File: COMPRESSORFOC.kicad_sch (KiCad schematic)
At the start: 85 parts, among them J1 ESP32-PICO-KIT_ESP32-PICO-KIT, J10 3.3V, J11 Pin 1, J12 Pin 2, J13 GND, J2 Fan 1+, J3 Fan 1-, J4 15V+, J5 15VGND, J6 Conn_01x03_Socket, J7 Conn_01x03_Socket, J8 Fan 2+, J9 Fan 2-, Q1 NMOSIPD50R280CEAUMA1, U2 INA240A2DR, U3 INA240A2DR, U5 INA240A2DR

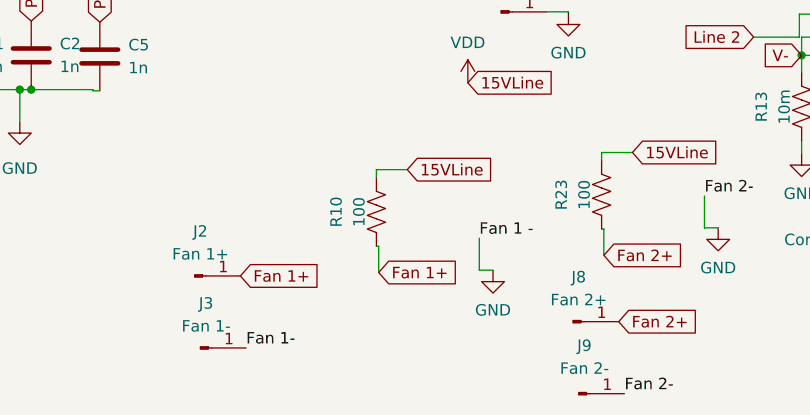
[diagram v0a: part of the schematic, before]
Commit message: workflow typo fix and some erc fixes
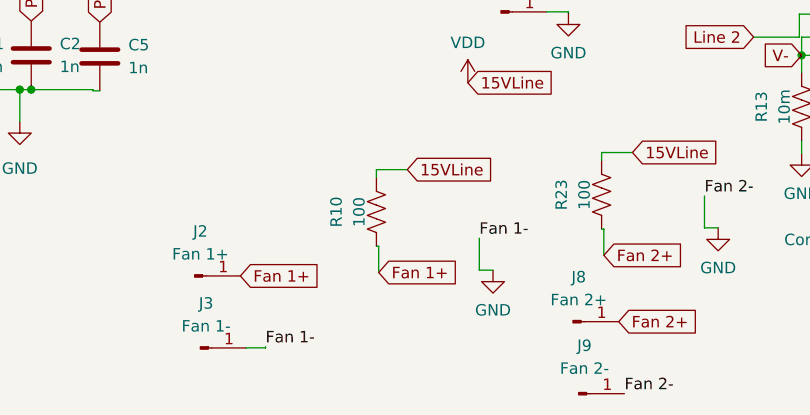
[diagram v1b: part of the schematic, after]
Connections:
- net Fan 1- is gone; now on net GND: J3.1 (Pin_1)
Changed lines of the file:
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@@
+    (stroke (width 0) (type default))
+  )
+  (wire (pts (xy 90.551 188.214) (xy 90.551 188.087))
     (stroke (width 0) (type default))
   )
@@
     (stroke (width 0) (type default))
   )
+  (wire (pts (xy 88.392 188.214) (xy 90.551 188.214))
+    (stroke (width 0) (type default))
+  )
   (wire (pts (xy 128.27 78.74) (xy 132.715 78.74))
     (stroke (width 0) (type default))
@@
     (stroke (width 0) (type default))
   )
-  (label "Fan 1 -" (at 114.3 176.022 0) (fields_autoplaced)
+  (label "Fan 1-" (at 114.3 176.022 0) (fields_autoplaced)
     (effects (font (size 1.27 1.27)) (justify left bottom))
   )
@@
     (effects (font (size 1.27 1.27)) (justify left bottom))
   )
-  (label "Fan 1-" (at 88.392 188.214 0) (fields_autoplaced)
+  (label "Fan 1-" (at 90.551 188.087 0) (fields_autoplaced)
     (effects (font (size 1.27 1.27)) (justify left bottom))
   )

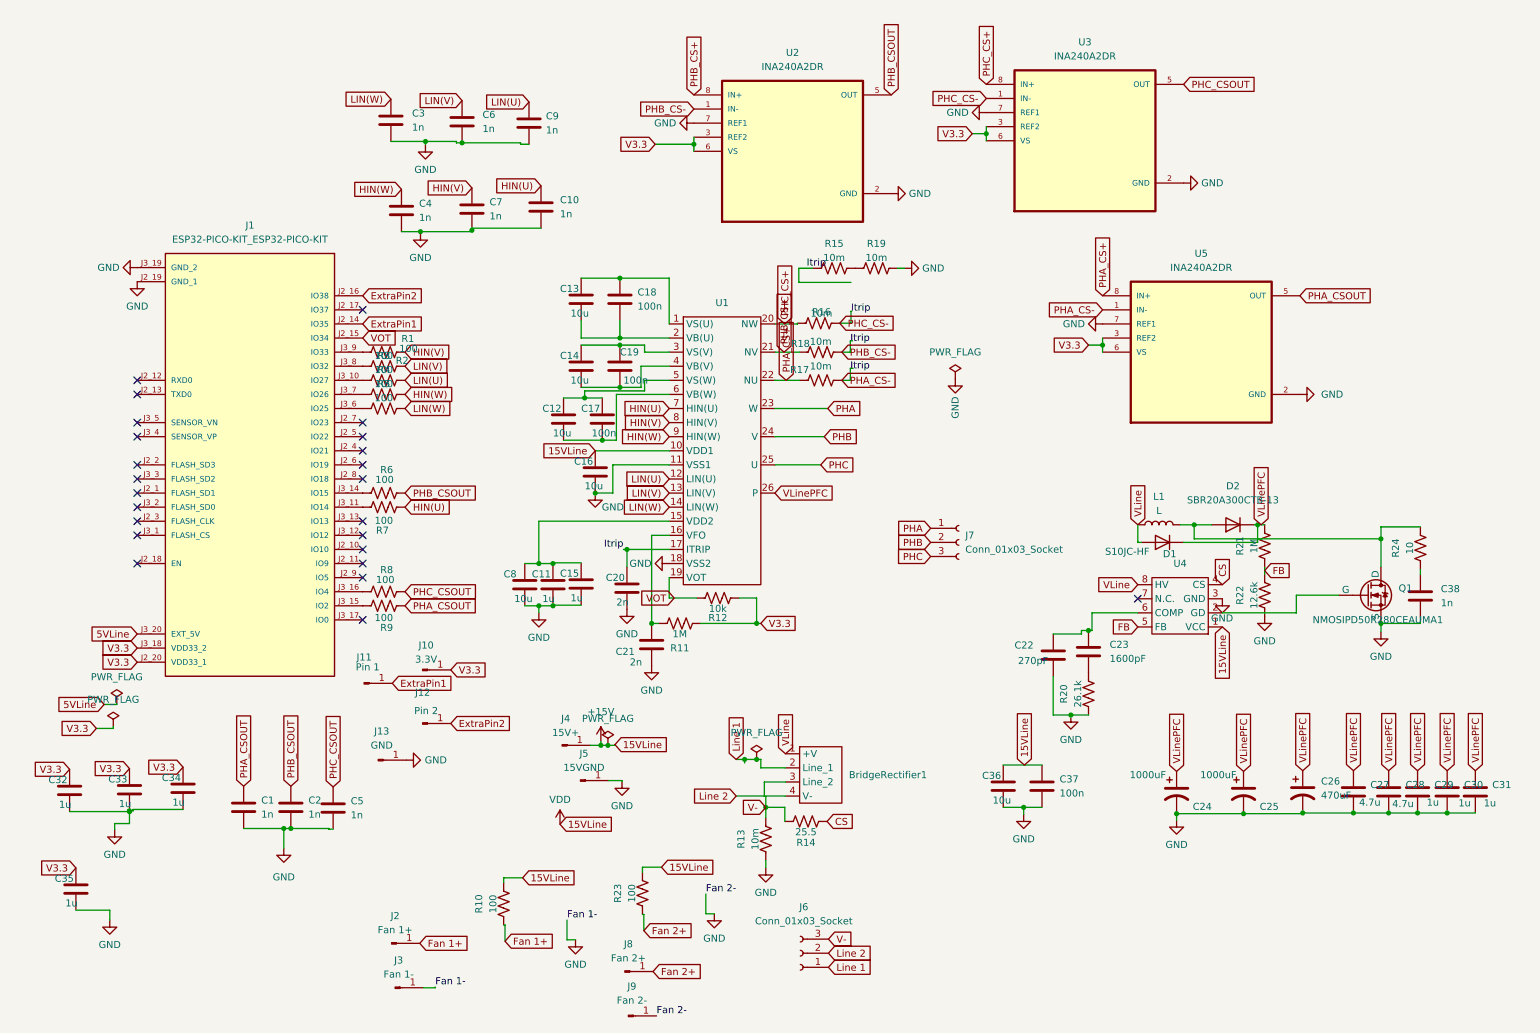
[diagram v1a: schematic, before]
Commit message: revised driver
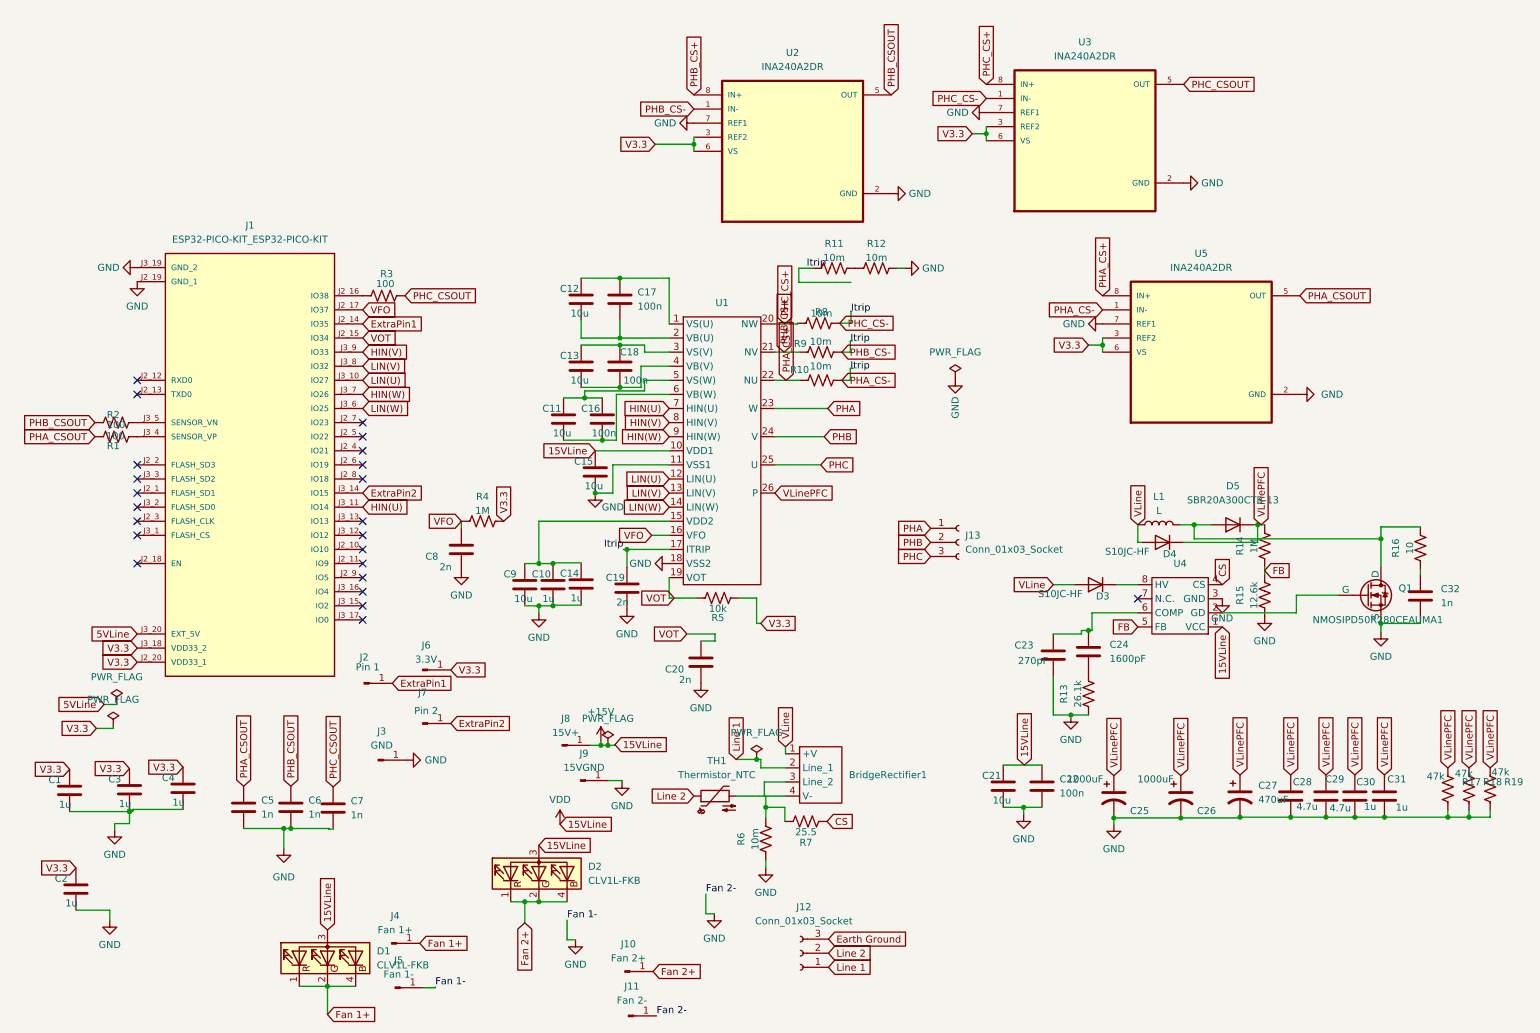
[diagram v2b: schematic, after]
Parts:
- removed C10, C3, C4, C6, C7, C9: 1n, Capacitor_SMD:C_0603_1608Metric_Pad1.08x0.95mm_HandSolder, symbol Device:C
- removed C31: 1u, Capacitor_SMD:C_1812_4532Metric_Pad1.57x3.40mm_HandSolder, symbol Device:C
- removed R1, R10, R2, R23, R3, R5, R7: 100, Resistor_SMD:R_0603_1608Metric_Pad0.98x0.95mm_HandSolder, symbol Device:R_US
- removed R11: 1M, Resistor_SMD:R_0805_2012Metric_Pad1.20x1.40mm_HandSolder, symbol Device:R_US
- added C8: 2n, Capacitor_SMD:C_0603_1608Metric_Pad1.08x0.95mm_HandSolder, symbol Device:C
- added D1, D2: CLV1L-FKB, LED_SMD:LED_Cree-PLCC4_3.2x2.8mm_CCW, symbol LED:CLV1L-FKB
- added D3: S10JC-HF, Diode_SMD:D_SMC_Handsoldering, symbol Device:D
- added R17, R18, R19: 47k, Resistor_SMD:R_2512_6332Metric_Pad1.40x3.35mm_HandSolder, symbol Device:R_US
- added TH1: Thermistor_NTC, COMPRESSORFOC:NTC_compressorfoc, symbol Device:Thermistor_NTC
- C30: renamed from C29; footprint Capacitor_SMD:C_1812_4532Metric_Pad1.57x3.40mm_HandSolder -> Capacitor_SMD:C_2225_5664Metric_Pad1.80x6.60mm_HandSolder
- C31: renamed from C30; footprint Capacitor_SMD:C_1812_4532Metric_Pad1.57x3.40mm_HandSolder -> Capacitor_SMD:C_2225_5664Metric_Pad1.80x6.60mm_HandSolder
- D5: renamed from D2; footprint COMPRESSORFOC:TO-252-2_DiodeFOCCustom -> COMPRESSORFOC:TO-263-2-FOC
- J12: renamed from J6; footprint COMPRESSORFOC:TerminalBlock3pin -> COMPRESSORFOC:IEC_plugin
- R4: value 100 -> 1M; footprint Resistor_SMD:R_0603_1608Metric_Pad0.98x0.95mm_HandSolder -> Resistor_SMD:R_0805_2012Metric_Pad1.20x1.40mm_HandSolder
- renumbered C32 to C1, C11 to C10, C12 to C11, C13 to C12, C14 to C13, C15 to C14, C16 to C15, C17 to C16, C18 to C17, C19 to C18, C20 to C19, C35 to C2, C21 to C20, C36 to C21, C37 to C22, C22 to C23, C23 to C24, C24 to C25, C25 to C26, C26 to C27, C27 to C28, C28 to C29, C33 to C3, C38 to C32, C34 to C4, C1 to C5, C2 to C6, C5 to C7, C8 to C9, D1 to D4, J8 to J10, J9 to J11, J7 to J13, J11 to J2, J13 to J3, J2 to J4, J3 to J5, J10 to J6, J12 to J7, J4 to J8, J5 to J9, R6 to R1, R17 to R10, R15 to R11, R19 to R12, R20 to R13, R21 to R14, R22 to R15, R24 to R16, R9 to R2, R8 to R3, R12 to R5, R13 to R6, R14 to R7, R16 to R8, R18 to R9
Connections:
- net +15V: now also D1.3 (A), D2.3 (A)
- net ExtraPin2: now also J1.J3_14 (IO15); no longer J1.J2_16 (IO38)
- net Fan 1+: now also D1.1 (RK), D1.2 (GK), D1.4 (BK)
- net Fan 2+: now also D2.1 (RK), D2.2 (GK), D2.4 (BK)
- net GND: now also C8.2, R17.2, R18.2, R19.2
- net HIN(U): now also J1.J3_11 (IO14)
- net HIN(V): now also J1.J3_9 (IO33)
- net HIN(W): now also J1.J3_7 (IO26); no longer R4.2
- net LIN(U): now also J1.J3_10 (IO27)
- net LIN(V): now also J1.J3_8 (IO32)
- net LIN(W): now also J1.J3_6 (IO25)
- net Line 2: now also TH1.1; no longer BridgeRectifier1.3 (Line_2)
- net V3.3: now also R4.2
- net VLine: now also D3.2 (A); no longer U4.8 (HV)
- net VLinePFC: now also R17.1, R18.1, R19.1
- net VOT: now also C20.1
- net VFO: now reaches R4.1
- net VFO: now also J1.J2_17 (IO37), U1.16 (VFO), C8.1; no longer J1.J3_7 (IO26)
- net at R1.1: now also J1.J3_5 (SENSOR_VN); no longer J1.J3_14 (IO15)
- net at J1.J3_15 (IO2): no longer R2.1
- net at R3.1: now also J1.J2_16 (IO38); no longer J1.J3_16 (IO4)
- net at J1.J3_4 (SENSOR_VP): now also R2.1
- net V-: no longer names the net of BridgeRectifier1.4 (V-), R6.2, R7.2
- net V-: no longer J12.3 (Pin_3)
- new net: BridgeRectifier1.3 (Line_2), TH1.2
- new net: D3.1 (K), U4.8 (HV)
- new net Earth Ground: J12.3 (Pin_3)
- no-connect marks 24 -> 23
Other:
- moved on the sheet: C20, C25, C26, C27, C28, C29, C30, C31, R1, R2, R3
